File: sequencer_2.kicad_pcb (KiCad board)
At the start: 2 copper layers, 116 x 110 mm, 98 parts, among them J1 EuroPower16 THT, Q10 BC338, Q3 BC338, Q4 BC338, Q5 BC338, Q6 BC338, Q7 BC338, Q8 BC338, Q9 BC338, U2 MCP6002-xP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

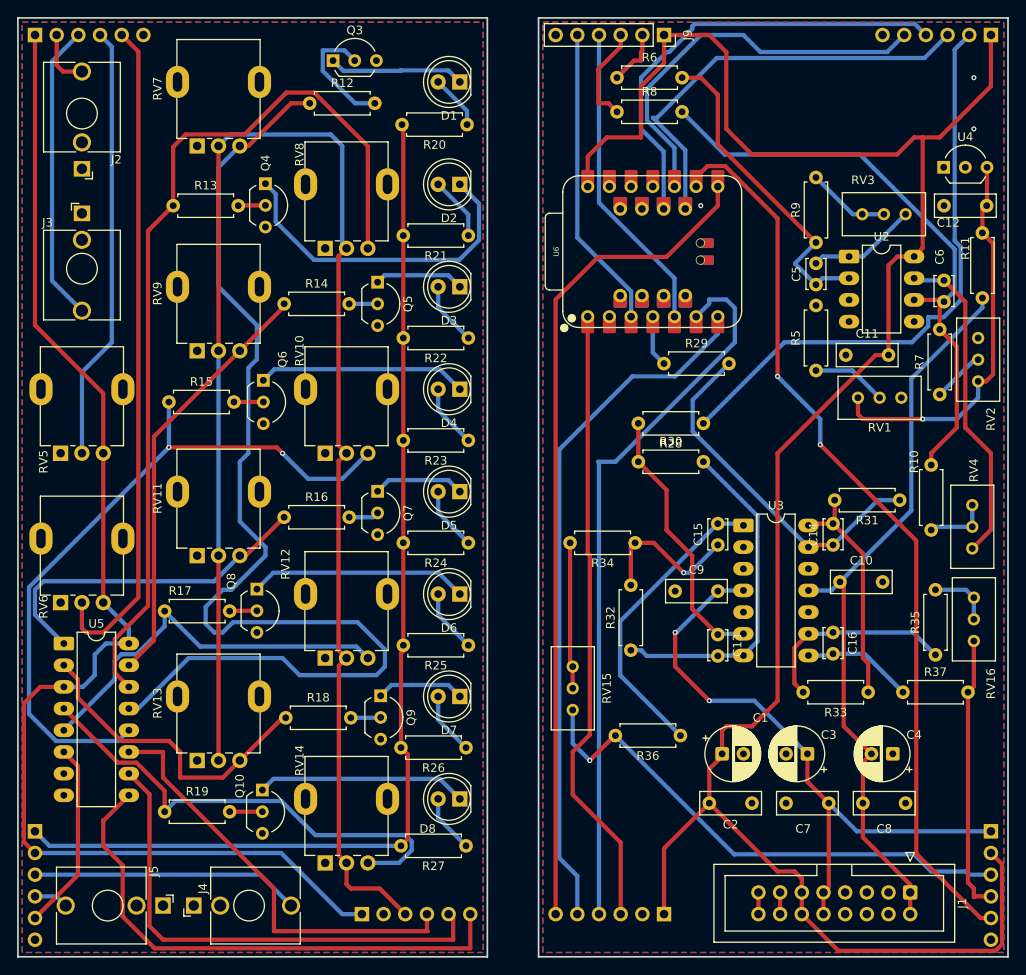
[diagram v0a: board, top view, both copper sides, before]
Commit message: J9 and J12 rework.
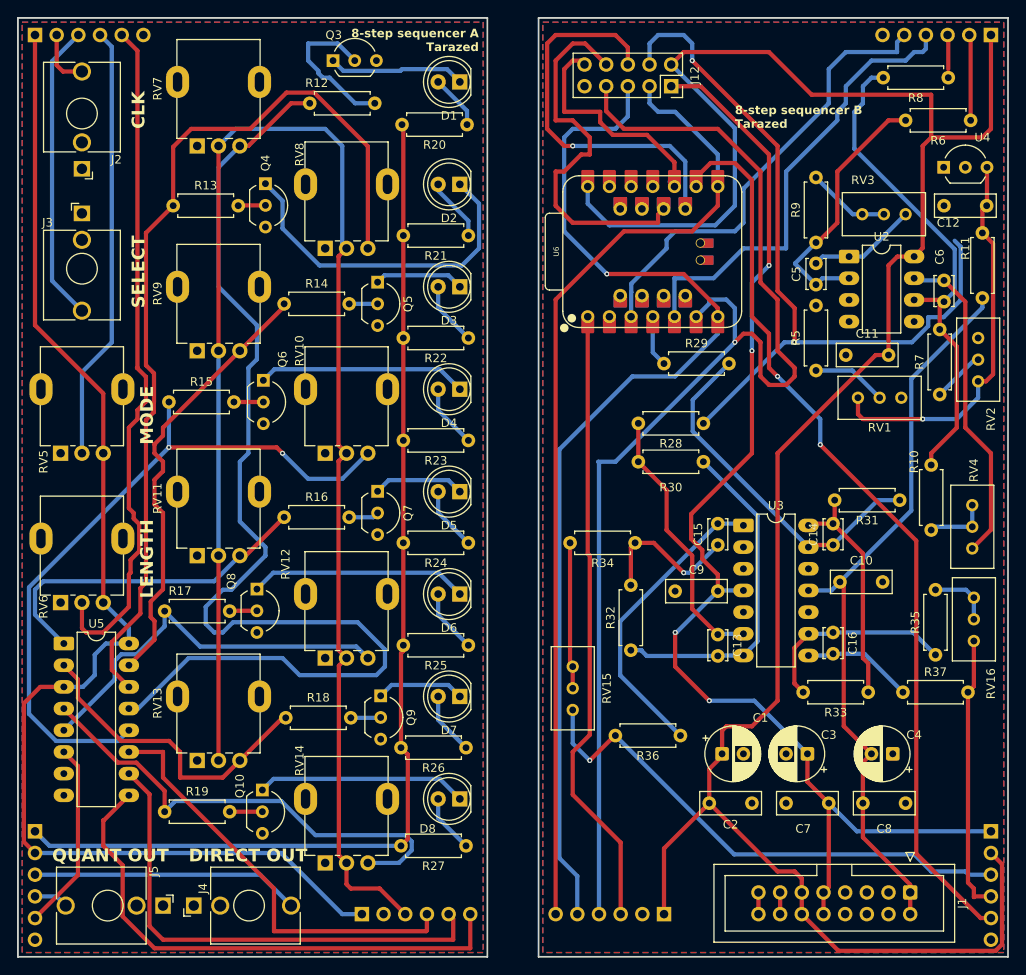
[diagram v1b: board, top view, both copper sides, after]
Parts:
- J12: footprint Connector_PinSocket_2.54mm:PinSocket_1x06_P2.54mm_Vertical -> Connector_PinSocket_2.54mm:PinSocket_2x05_P2.54mm_Vertical; moved to F.Cu
- J9: moved to B.Cu
- moved R6 41.7 mm to (161.6, 47.0), turned to 180 degrees
- moved R8 39.0 mm to (159.0, 42.0), turned to 180 degrees
- moved J9 38.3 mm to (164.0, 37.0), turned to 90 degrees
- moved J12 37.9 mm to (126.5, 43.0), turned to -90 degrees
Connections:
- J12 pad 1: +5V -> +12V
- J12 pad 2: CURRENT_CV -> +5V
- J12 pad 3: Q6 -> Q2_B
- J12 pad 4: Q5 -> CURRENT_CV
- J12 pad 5: Q4 -> Q1_B
- J12 pad 6: GND -> Q6
- J7 pad 4: Net-(J7-Pin_4) -> Q0_B
- J7 pad 5: Net-(J7-Pin_5) -> Q1_B
- J7 pad 6: Net-(J7-Pin_6) -> Q2_B
- U6 pad 6: Net-(J7-Pin_4) -> Q0_B
- U6 pad 7: Net-(J7-Pin_5) -> Q1_B
- U6 pad 8: Net-(J7-Pin_6) -> Q2_B
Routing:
- net Q0_B: track 0.00 -> 147.1 mm, vias 0 -> 1
- net Q1_B: track 0.00 -> 127.2 mm, vias 0 -> 1
- net Q2_B: track 0.00 -> 114.0 mm
- net Net-(J7-Pin_6): track 97.8 -> 0.00 mm
- net Net-(J7-Pin_4): track 84.9 -> 0.00 mm
- net Net-(J7-Pin_5): track 81.5 -> 0.00 mm
- net +12V: track 74.2 -> 145.2 mm, vias 2 -> 4
- net CURRENT_CV: track 68.8 -> 92.2 mm, vias 0 -> 2
- net Q4: track 48.0 -> 26.9 mm
- net LENGTH: track 35.6 -> 53.9 mm
- net MODE: track 36.7 -> 53.7 mm
- net +5V: track 244.5 -> 260.6 mm
- net Net-(U2B--): track 70.3 -> 58.8 mm
- net Q5: track 53.2 -> 45.1 mm
- net 2B: track 11.7 -> 4.03 mm
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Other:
- board text added: "8-step sequencer A Tarazed"
- board text added: "8-step sequencer B Tarazed"
- board text added: "CLK"
- board text added: "DIRECT OUT"
- board text added: "LENGTH"
- board text added: "MODE"
- board text added: "QUANT OUT"
- board text added: "SELECT"

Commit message: RST input.
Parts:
- added C17: 1n, Capacitor_THT:C_Disc_D3.4mm_W2.1mm_P2.50mm, F.Cu at (162.5, 67.8)
- added J13: ~, EuroRackTools:Jack_3.5mm_QingPu_WQP-PJ398SM_Vertical_CircularHoles, F.Cu at (64.0, 66.0)
- added R1: 100k, Resistor_THT:R_Axial_DIN0207_L6.3mm_D2.5mm_P7.62mm_Horizontal, F.Cu at (152.5, 55.4)
- added R2: 100k, Resistor_THT:R_Axial_DIN0207_L6.3mm_D2.5mm_P7.62mm_Horizontal, F.Cu at (153.0, 44.2)
- added R3: 47k, Resistor_THT:R_Axial_DIN0207_L6.3mm_D2.5mm_P7.62mm_Horizontal, F.Cu at (155.2, 62.6)
- added RV17: 100k, Potentiometer_THT:Potentiometer_Bourns_3296W_Vertical, F.Cu at (148.0, 61.7)
- added RV18: 100k, Potentiometer_THT:Potentiometer_Bourns_3296W_Vertical, F.Cu at (161.9, 57.9)
- J8: footprint Connector_PinHeader_2.54mm:PinHeader_1x06_P2.54mm_Vertical -> Connector_PinHeader_2.54mm:PinHeader_1x07_P2.54mm_Vertical
- J9: footprint Connector_PinSocket_2.54mm:PinSocket_1x06_P2.54mm_Vertical -> Connector_PinSocket_2.54mm:PinSocket_1x07_P2.54mm_Vertical
- U2: value MCP6002-xP -> MCP6004-xP; footprint Package_DIP:DIP-8_W7.62mm_LongPads -> Package_DIP:DIP-14_W7.62mm_LongPads
- moved RV3 32.1 mm to (143.9, 89.7), turned to -90 degrees
- moved U4 29.3 mm to (133.0, 38.0)
- moved C12 27.7 mm to (135.5, 41.6)
- moved R11 25.6 mm to (143.6, 43.5)
- moved R9 15.7 mm to (146.3, 76.8), turned to 180 degrees
- moved RV2 14.2 mm to (155.0, 84.6)
- moved U2 11.2 mm to (143.9, 73.6), turned to 90 degrees
- moved R10 10.6 mm to (156.7, 76.8), turned to 0 degrees
- moved J2 9.32 mm to (64.0, 46.0), turned to -90 degrees
- moved R8 8.85 mm to (156.4, 50.4), turned to 0 degrees
- moved R5 8.61 mm to (151.2, 80.3), turned to 180 degrees
- moved C11 7.49 mm to (154.1, 76.8), turned to 180 degrees
- moved R6 7.01 mm to (161.5, 40.0), turned to -90 degrees
- moved J3 6.77 mm to (64.0, 56.0), turned to -90 degrees
- moved RV1 6.50 mm to (149.4, 84.6), turned to 90 degrees
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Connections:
- C5 pad 2: CLK_A -> CLK
- C6 pad 2: SELECT_A -> SELECT
- J8 pad 4: Net-(J8-Pin_4) -> 3A
- J8 pad 6: GND_A -> Net-(J8-Pin_6)
- J9 pad 4: MODE -> 3B
- J9 pad 5: LENGTH -> MODE
- J9 pad 6: GND -> LENGTH
- RV3 pad 3: CLK_A -> CLK
- RV4 pad 3: SELECT_A -> SELECT
- RV5 pad 2: Net-(J8-Pin_4) -> Net-(J8-Pin_5)
- RV6 pad 2: Net-(J8-Pin_5) -> Net-(J8-Pin_6)
- U2 pad 1: CLK_A -> CLK
- U2 pad 4: GND -> +5V
- U2 pad 7: SELECT_A -> SELECT
- U2 pad 8: +5V -> RST
- U6 pad 11: CLK_B -> CLK
- U6 pad 19: unconnected-(U6-P101_D15_MOSI0-Pad19) -> RST
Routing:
- net 3A: track 31.5 -> 141.7 mm, vias 0 -> 3
- net 3B: track 61.7 -> 164.1 mm, vias 1 -> 3
- net SELECT: track 0.00 -> 92.2 mm, vias 0 -> 1
- net Net-(J8-Pin_6): track 0.00 -> 90.4 mm
- net CLK: track 0.00 -> 86.3 mm, vias 0 -> 2
- net -12V: track 87.4 -> 158.8 mm
- net RST: track 0.00 -> 62.0 mm
- net Net-(J8-Pin_4): track 51.0 -> 0.00 mm
- net SELECT_A: track 38.2 -> 0.00 mm
- net +5V: track 260.6 -> 295.9 mm, vias 0 -> 1
- net Net-(U2C--): track 0.00 -> 26.4 mm
- net Net-(J8-Pin_5): track 80.0 -> 53.8 mm
- net A_REF_-10V: track 46.3 -> 72.4 mm
- net CURRENT_CV: track 92.2 -> 66.5 mm, vias 2 -> 3
- net Net-(U2A--): track 31.1 -> 53.2 mm
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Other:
- board text added: "RST"
- board text added: "SEL"
- board text removed: "SELECT"
